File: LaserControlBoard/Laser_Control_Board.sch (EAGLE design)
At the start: 37 parts, among them IC1 ULN2803, J1 Servo, J2 FTDI, J5 FEMALE 2x3, Q1 BUK9880-55A, Q2 BUK9880-55A, U1 ATMEGA328P, Y1 16MHz

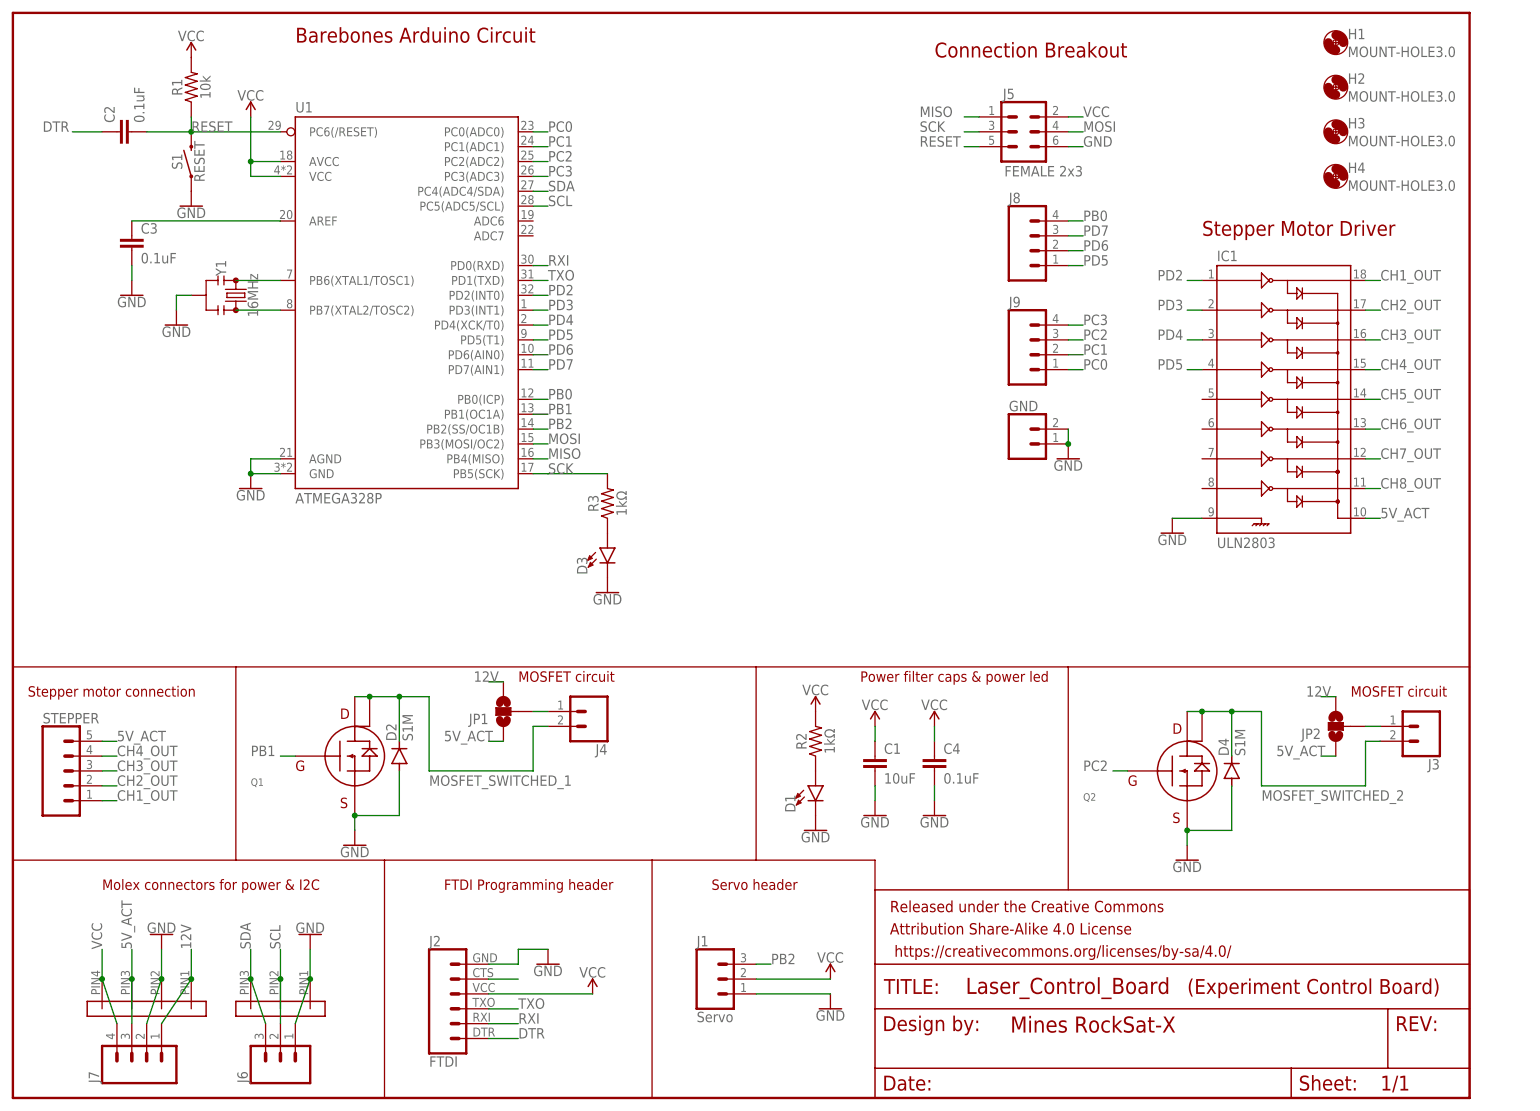
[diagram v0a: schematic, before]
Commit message: Initial Rev2 for Boom and Exp. Control boards
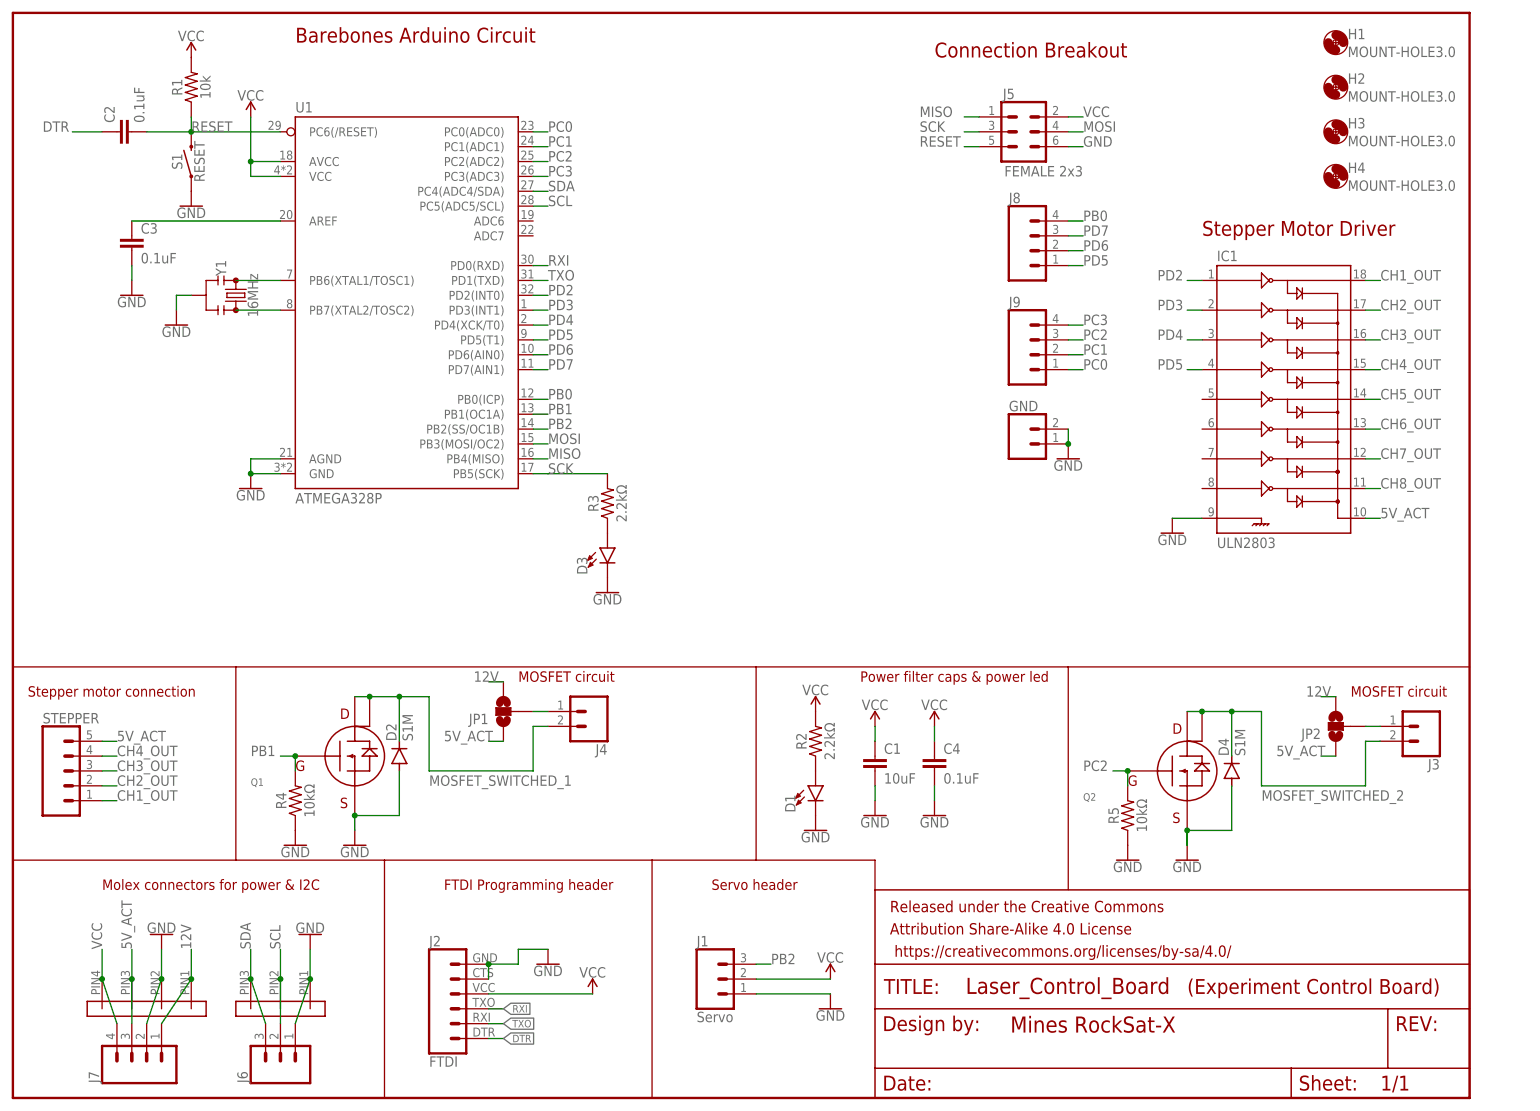
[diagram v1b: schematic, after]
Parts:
- added R4, R5: 10kΩ, SparkFun-Resistors:RESISTOR0805
- R2, R3: value 1kΩ -> 2.2kΩ
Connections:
- removed net N$6: J2.5
- net GND: now also J2.5, R4.1, R5.1
- net PB1: now also R4.2
- net PC2: now also R5.2
- net RXI: now also J2.3; no longer J2.2
- net TXO: now also J2.2; no longer J2.3
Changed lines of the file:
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@@
 <?xml version="1.0" encoding="utf-8"?>
 <!DOCTYPE eagle SYSTEM "eagle.dtd">
-<eagle version="9.4.2">
+<eagle version="9.5.2">
 <drawing>
 <settings>
@@
 <part name="SUPPLY8" library="SparkFun-PowerSymbols" deviceset="VCC" device=""/>
 <part name="GND11" library="SparkFun-PowerSymbols" deviceset="GND" device=""/>
-<part name="R2" library="SparkFun-Resistors" deviceset="RESISTOR" device="0805" value="1kΩ"/>
+<part name="R2" library="SparkFun-Resistors" deviceset="RESISTOR" device="0805" value="2.2kΩ"/>
 <part name="STEPPER" library="SparkFun-Connectors" deviceset="CONN_05" device=""/>
 <part name="GND12" library="SparkFun-PowerSymbols" deviceset="GND" device=""/>
@@
 <part name="J4" library="SparkFun-Connectors" deviceset="CONN_02" device=""/>
 <part name="GND1" library="SparkFun-PowerSymbols" deviceset="GND" device=""/>
-<part name="R3" library="SparkFun-Resistors" deviceset="RESISTOR" device="0805" value="1kΩ"/>
+<part name="R3" library="SparkFun-Resistors" deviceset="RESISTOR" device="0805" value="2.2kΩ"/>
 <part name="D3" library="SparkFun-LED" deviceset="LED-GREEN" device="1206"/>
 <part name="GND14" library="SparkFun-PowerSymbols" deviceset="GND" device=""/>
@@
 <part name="GND" library="SparkFun-Connectors" deviceset="CONN_02" device="LOCK_LONGPADS"/>
 <part name="GND16" library="SparkFun-PowerSymbols" deviceset="GND" device=""/>
+<part name="R4" library="SparkFun-Resistors" deviceset="RESISTOR" device="0805" value="10kΩ"/>
+<part name="GND17" library="SparkFun-PowerSymbols" deviceset="GND" device=""/>
+<part name="R5" library="SparkFun-Resistors" deviceset="RESISTOR" device="0805" value="10kΩ"/>
+<part name="GND18" library="SparkFun-PowerSymbols" deviceset="GND" device=""/>
 </parts>
 <sheets>
@@
 <attribute name="VALUE" x="180.34" y="108.966" size="1.778" layer="96" align="top-center"/>
 </instance>
+<instance part="R4" gate="G$1" x="48.26" y="50.8" smashed="yes" rot="R90">
+<attribute name="NAME" x="46.736" y="50.8" size="1.778" layer="95" font="vector" rot="R90" align="bottom-center"/>
+<attribute name="VALUE" x="49.784" y="50.8" size="1.778" layer="96" font="vector" rot="R90" align="top-center"/>
+</instance>
+<instance part="GND17" gate="1" x="48.26" y="43.18" smashed="yes">
+<attribute name="VALUE" x="48.26" y="42.926" size="1.778" layer="96" align="top-center"/>
+</instance>
+<instance part="R5" gate="G$1" x="190.5" y="48.26" smashed="yes" rot="R90">
+<attribute name="NAME" x="188.976" y="48.26" size="1.778" layer="95" font="vector" rot="R90" align="bottom-center"/>
+<attribute name="VALUE" x="192.024" y="48.26" size="1.778" layer="96" font="vector" rot="R90" align="top-center"/>
+</instance>
+<instance part="GND18" gate="1" x="190.5" y="40.64" smashed="yes">
+<attribute name="VALUE" x="190.5" y="40.386" size="1.778" layer="96" align="top-center"/>
+</instance>
 </instances>
 <busses>
@@
 <pinref part="GND4" gate="1" pin="GND"/>
 <wire x1="86.36" y1="25.4" x2="91.44" y2="25.4" width="0.1524" layer="91"/>
+<pinref part="J2" gate="G$1" pin="5"/>
+<wire x1="81.28" y1="20.32" x2="81.28" y2="22.86" width="0.1524" layer="91"/>
+<junction x="81.28" y="22.86"/>
 </segment>
 <segment>
@@
 <junction x="200.66" y="45.72"/>
 <pinref part="GND15" gate="1" pin="GND"/>
+<wire x1="200.66" y1="45.72" x2="200.66" y2="43.18" width="0.1524" layer="91"/>
 </segment>
 <segment>
@@
 <junction x="180.34" y="111.76"/>
 </segment>
+<segment>
+<pinref part="R4" gate="G$1" pin="1"/>
+<pinref part="GND17" gate="1" pin="GND"/>
+</segment>
+<segment>
+<pinref part="R5" gate="G$1" pin="1"/>
+<pinref part="GND18" gate="1" pin="GND"/>
+</segment>
 </net>
 <net name="DTR" class="0">
@@
 <segment>
 <pinref part="J2" gate="G$1" pin="1"/>
-<wire x1="81.28" y1="10.16" x2="86.36" y2="10.16" width="0.1524" layer="91"/>
-<label x="86.36" y="10.16" size="1.778" layer="95"/>
+<wire x1="81.28" y1="10.16" x2="83.82" y2="10.16" width="0.1524" layer="91"/>
+<label x="83.82" y="10.16" size="1.27" layer="95" xref="yes"/>
 </segment>
 </net>
 <net name="RXI" class="0">
-<segment>
-<pinref part="J2" gate="G$1" pin="2"/>
-<wire x1="81.28" y1="12.7" x2="86.36" y2="12.7" width="0.1524" layer="91"/>
-<label x="86.36" y="12.7" size="1.778" layer="95"/>
-</segment>
 <segment>
 <pinref part="U1" gate="U1" pin="PD0(RXD)"/>
@@
 <label x="91.44" y="142.24" size="1.778" layer="95"/>
 </segment>
+<segment>
+<pinref part="J2" gate="G$1" pin="3"/>
+<wire x1="81.28" y1="15.24" x2="83.82" y2="15.24" width="0.1524" layer="91"/>
+<label x="83.82" y="15.24" size="1.27" layer="95" xref="yes"/>
+</segment>
 </net>
 <net name="TXO" class="0">
-<segment>
-<pinref part="J2" gate="G$1" pin="3"/>
-<wire x1="81.28" y1="15.24" x2="86.36" y2="15.24" width="0.1524" layer="91"/>
-<label x="86.36" y="15.24" size="1.778" layer="95"/>
-</segment>
 <segment>
 <pinref part="U1" gate="U1" pin="PD1(TXD)"/>
@@
 <label x="91.44" y="139.7" size="1.778" layer="95"/>
 </segment>
-</net>
-<net name="N$6" class="0">
-<segment>
-<pinref part="J2" gate="G$1" pin="5"/>
-<wire x1="81.28" y1="20.32" x2="86.36" y2="20.32" width="0.1524" layer="91"/>
+<segment>
+<pinref part="J2" gate="G$1" pin="2"/>
+<wire x1="81.28" y1="12.7" x2="83.82" y2="12.7" width="0.1524" layer="91"/>
+<label x="83.82" y="12.7" size="1.27" layer="95" xref="yes"/>
 </segment>
 </net>
@@
 <segment>
 <pinref part="Q1" gate="G$1" pin="GATE"/>
+<label x="40.64" y="58.42" size="1.778" layer="95"/>
+<pinref part="R4" gate="G$1" pin="2"/>
+<junction x="48.26" y="58.42"/>
+<wire x1="48.26" y1="55.88" x2="48.26" y2="58.42" width="0.1524" layer="91"/>
 <wire x1="48.26" y1="58.42" x2="45.72" y2="58.42" width="0.1524" layer="91"/>
-<label x="40.64" y="58.42" size="1.778" layer="95"/>
 </segment>
 </net>
@@
 <wire x1="190.5" y1="55.88" x2="187.96" y2="55.88" width="0.1524" layer="91"/>
 <label x="182.88" y="55.88" size="1.778" layer="95"/>
-</segment>
-<segment>
+<pinref part="R5" gate="G$1" pin="2"/>
+<wire x1="190.5" y1="53.34" x2="190.5" y2="55.88" width="0.1524" layer="91"/>
+<junction x="190.5" y="55.88"/>
+</segment>
+<segment>

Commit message: edits to exp and boom control boards
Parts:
- added JP3: JUMPER-SMT_3_NO_NO_SILK, SparkFun-Jumpers:JUMPER-SMT_3_NO_NO_SILK
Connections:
- new net N$6: IC1.10, JP3.2, STEPPER.5
- net 12V: now also JP3.3
- net 5V_ACT: now also JP3.1; no longer IC1.10, STEPPER.5
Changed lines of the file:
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@@
 <part name="R5" library="SparkFun-Resistors" deviceset="RESISTOR" device="0805" value="10kΩ"/>
 <part name="GND18" library="SparkFun-PowerSymbols" deviceset="GND" device=""/>
+<part name="JP3" library="SparkFun-Jumpers" deviceset="JUMPER-SMT_3_NO" device="_NO_SILK" value=""/>
 </parts>
 <sheets>
@@
 <attribute name="VALUE" x="190.5" y="40.386" size="1.778" layer="96" align="top-center"/>
 </instance>
+<instance part="JP3" gate="G$1" x="238.76" y="96.52" smashed="yes">
+<attribute name="NAME" x="241.3" y="96.901" size="1.778" layer="95" font="vector"/>
+<attribute name="VALUE" x="241.3" y="96.139" size="1.778" layer="96" font="vector" align="top-left"/>
+</instance>
 </instances>
 <busses>
@@
 <pinref part="JP2" gate="G$1" pin="3"/>
 </segment>
+<segment>
+<pinref part="JP3" gate="G$1" pin="3"/>
+<wire x1="238.76" y1="91.44" x2="241.3" y2="91.44" width="0.1524" layer="91"/>
+<label x="241.3" y="91.44" size="1.27" layer="95"/>
+</segment>
 </net>
 <net name="5V_ACT" class="0">
@@
 </segment>
 <segment>
-<pinref part="IC1" gate="G$1" pin="10"/>
-<wire x1="231.14" y1="99.06" x2="233.68" y2="99.06" width="0.1524" layer="91"/>
-<label x="233.68" y="99.06" size="1.778" layer="95"/>
-</segment>
-<segment>
-<pinref part="STEPPER" gate="G$1" pin="5"/>
-<wire x1="15.24" y1="60.96" x2="17.78" y2="60.96" width="0.1524" layer="91"/>
-<label x="17.78" y="60.96" size="1.778" layer="95"/>
-</segment>
-<segment>
 <wire x1="83.82" y1="60.96" x2="81.28" y2="60.96" width="0.1524" layer="91"/>
 <label x="73.66" y="60.96" size="1.778" layer="95"/>
@@
 <label x="215.9" y="58.42" size="1.778" layer="95"/>
 <pinref part="JP2" gate="G$1" pin="1"/>
+</segment>
+<segment>
+<pinref part="JP3" gate="G$1" pin="1"/>
+<wire x1="238.76" y1="101.6" x2="241.3" y2="101.6" width="0.1524" layer="91"/>
+<label x="241.3" y="101.6" size="1.27" layer="95"/>
 </segment>
 </net>
@@
 </segment>
 </net>
+<net name="N$6" class="0">
+<segment>
+<pinref part="IC1" gate="G$1" pin="10"/>
+<pinref part="JP3" gate="G$1" pin="2"/>
+<wire x1="231.14" y1="99.06" x2="233.68" y2="99.06" width="0.1524" layer="91"/>
+<wire x1="233.68" y1="99.06" x2="233.68" y2="96.52" width="0.1524" layer="91"/>
+</segment>
+<segment>
+<pinref part="STEPPER" gate="G$1" pin="5"/>
+<wire x1="15.24" y1="60.96" x2="17.78" y2="60.96" width="0.1524" layer="91"/>
+<label x="17.78" y="60.96" size="1.778" layer="95"/>
+</segment>
+</net>
